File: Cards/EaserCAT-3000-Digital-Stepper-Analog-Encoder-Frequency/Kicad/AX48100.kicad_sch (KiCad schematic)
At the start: 34 parts, among them U10 AX58100, U8 24LC32A, Y2 NXK25.000AE12F-KAB6-12

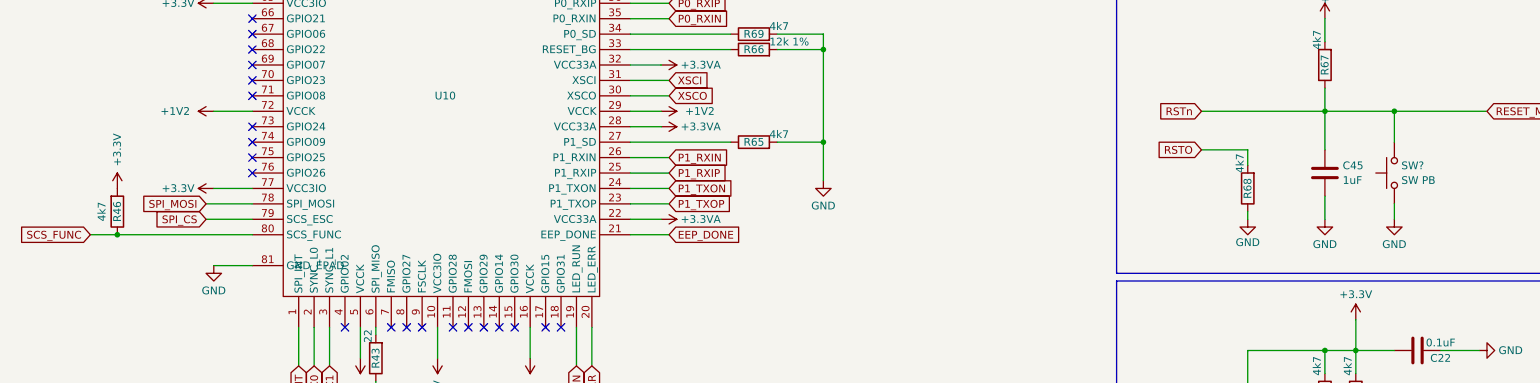
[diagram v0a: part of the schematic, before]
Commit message: Moving all to Kicad8. Housekeeping symbols,libraries,3d-models
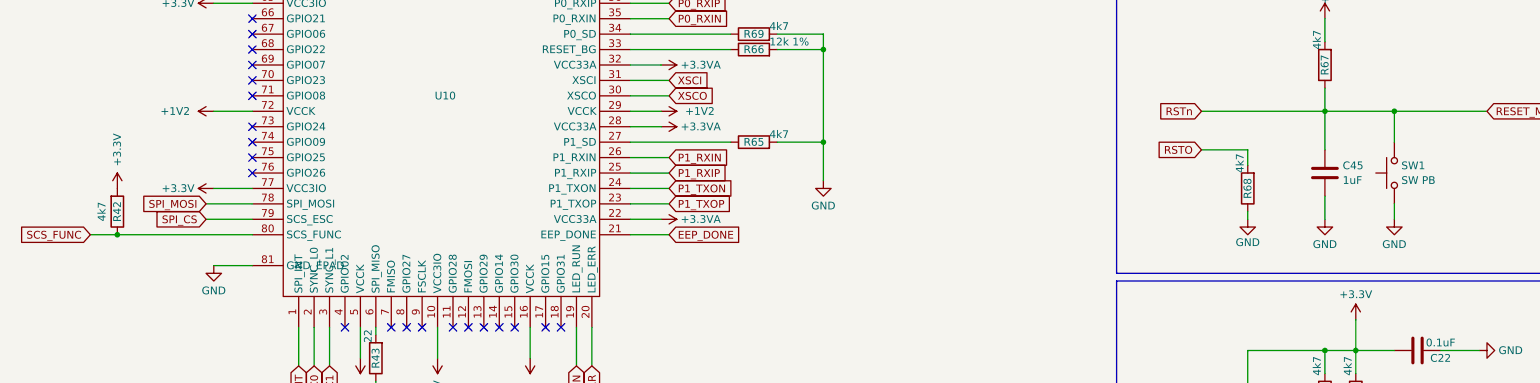
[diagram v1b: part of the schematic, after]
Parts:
- gave numbers to parts that had none: 1
- renumbered R46 to R42
